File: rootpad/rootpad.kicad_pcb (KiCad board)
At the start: 2 copper layers, 76.2 x 99.2 mm, 56 parts, among them J1 USB_B_Mini, SW1 SW_Push, U1 ATmega32U4-AU, Y1 16MHz

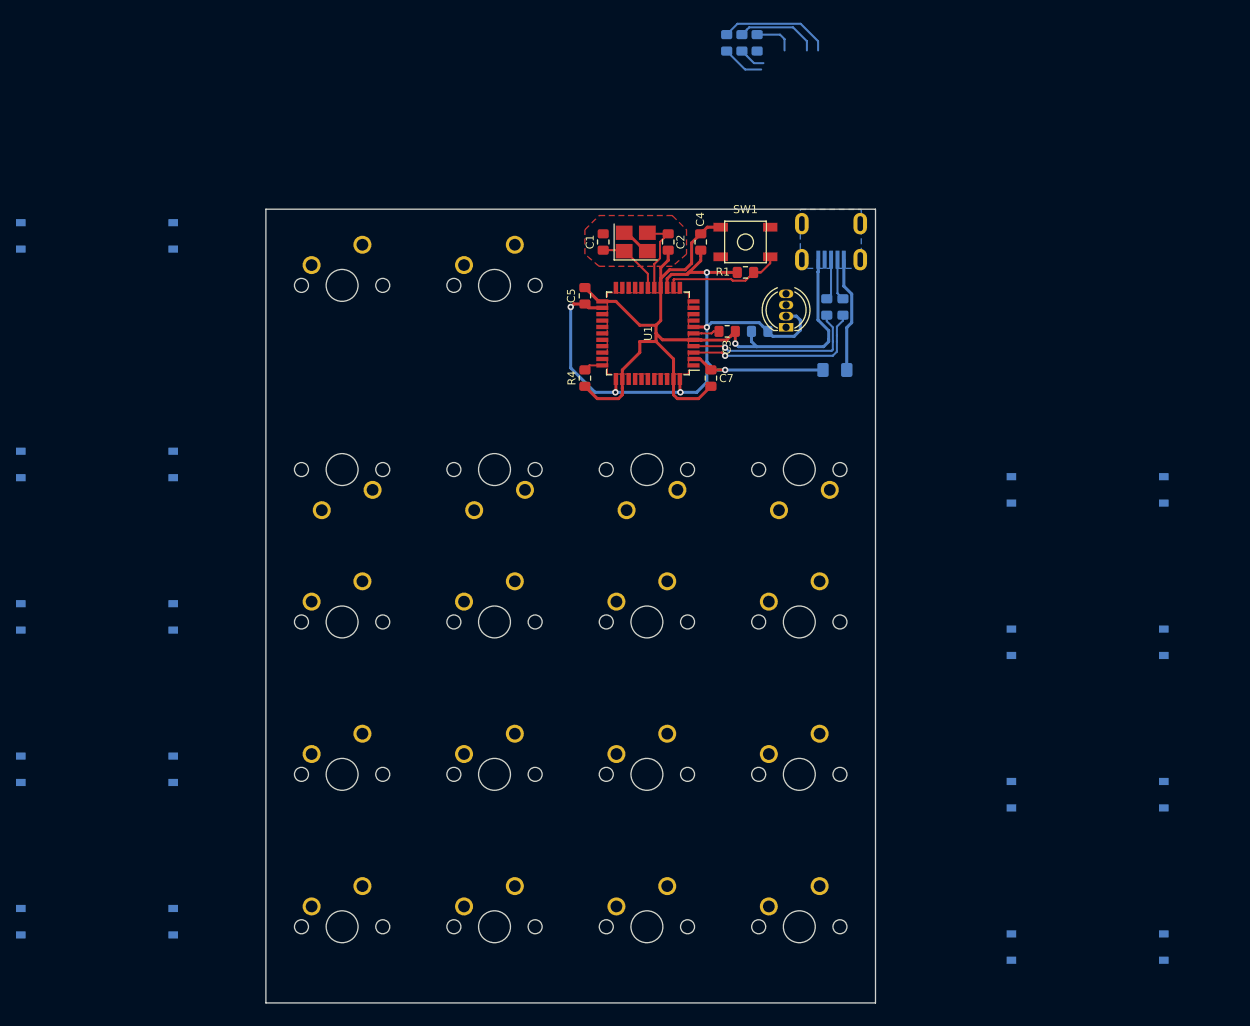
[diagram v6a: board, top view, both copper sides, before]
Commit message: Routed matrix and LED
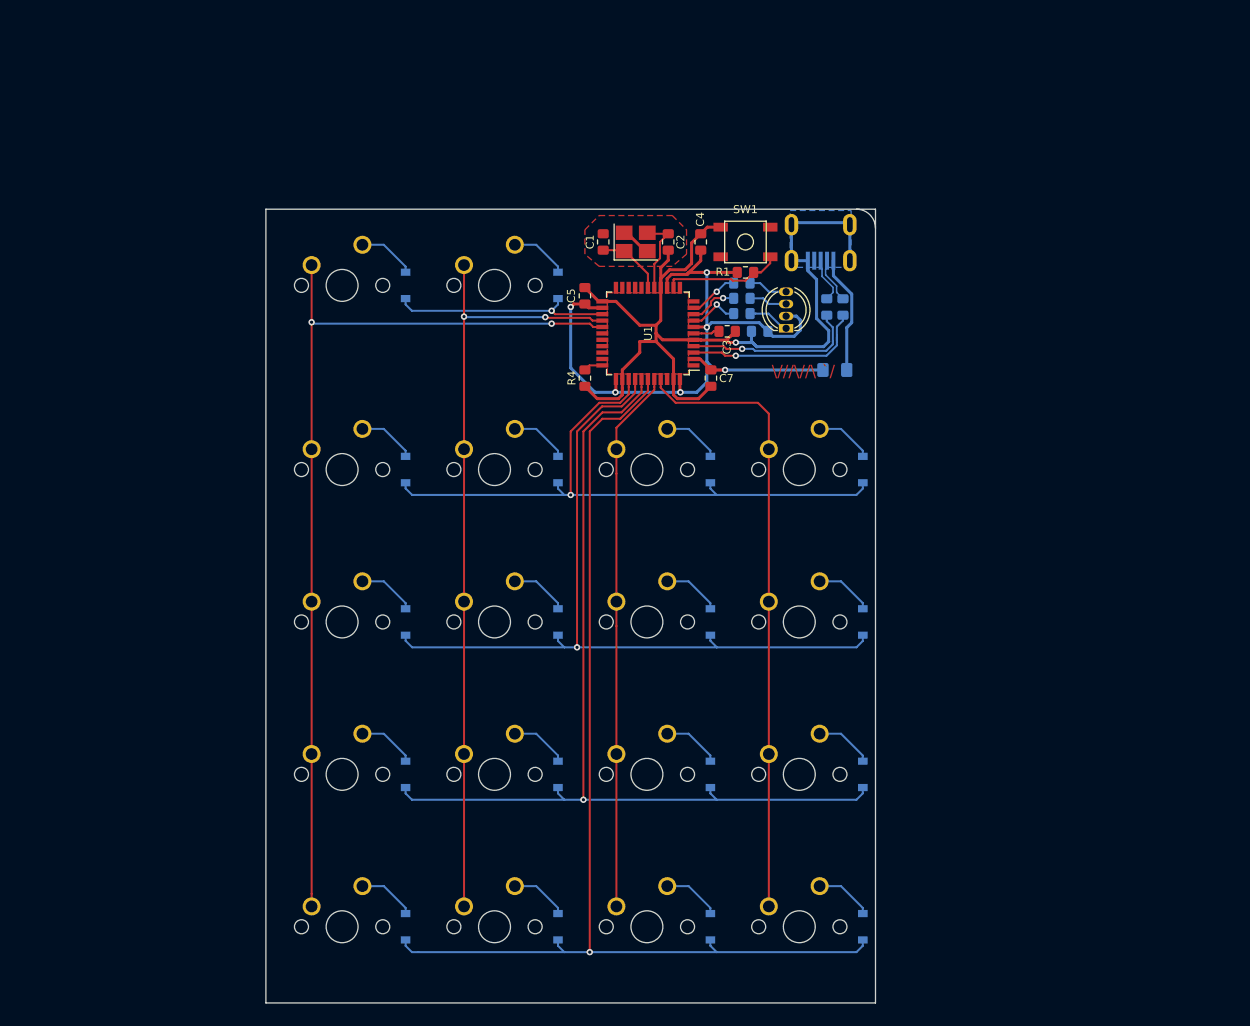
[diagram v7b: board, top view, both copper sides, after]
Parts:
- moved D1 48.5 mm to (138.1, 65.9)
- moved D2 48.5 mm to (157.2, 65.9)
- moved D11 48.1 mm to (138.1, 127.0)
- moved D15 48.1 mm to (138.1, 146.1)
- moved D3 48.1 mm to (138.1, 88.9)
- moved D7 48.1 mm to (138.1, 108.0)
- moved D12 48.1 mm to (157.2, 127.0)
- moved D16 48.1 mm to (157.2, 146.1)
- moved D4 48.1 mm to (157.2, 88.9)
- moved D8 48.1 mm to (157.2, 108.0)
- moved D10 37.7 mm to (195.3, 108.0)
- moved D13 37.7 mm to (176.2, 127.0)
- moved D14 37.7 mm to (195.3, 127.0)
- moved D18 37.7 mm to (195.3, 146.1)
- moved D6 37.7 mm to (195.3, 88.9)
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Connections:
- U1 pad 10: Net-(U1-Pad10) -> LED_B
- U1 pad 25: Net-(U1-Pad25) -> ROW0
- U1 pad 26: Net-(U1-Pad26) -> COL1
- U1 pad 27: Net-(U1-Pad27) -> COL0
- U1 pad 36: Net-(U1-Pad36) -> ROW1
- U1 pad 37: Net-(U1-Pad37) -> ROW2
- U1 pad 38: Net-(U1-Pad38) -> ROW3
- U1 pad 39: Net-(U1-Pad39) -> ROW4
- U1 pad 40: Net-(U1-Pad40) -> COL2
- U1 pad 41: Net-(U1-Pad41) -> COL3
- U1 pad 8: Net-(U1-Pad8) -> LED_R
- U1 pad 9: Net-(U1-Pad9) -> LED_G
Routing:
- net ROW4: track 0.00 -> 138.9 mm, vias 0 -> 1
- net ROW3: track 0.00 -> 120.0 mm, vias 0 -> 1
- net COL0: track 0.00 -> 116.8 mm, vias 0 -> 2
- net ROW2: track 0.00 -> 100.9 mm, vias 0 -> 1
- net COL1: track 0.00 -> 97.7 mm, vias 0 -> 2
- net ROW1: track 0.00 -> 82.0 mm, vias 0 -> 1
- net COL3: track 0.00 -> 77.6 mm
- net COL2: track 0.00 -> 67.9 mm
- net ROW0: track 0.00 -> 27.7 mm, vias 0 -> 1
- net GND: track 105.1 -> 123.5 mm
- net Net-(D19-Pad4): track 14.0 -> 4.95 mm
- net Net-(D2-Pad2): track 0.00 -> 7.23 mm
- net Net-(D1-Pad2): track 0.00 -> 7.23 mm
- net Net-(D18-Pad2): track 0.00 -> 7.23 mm
- net Net-(D17-Pad2): track 0.00 -> 7.23 mm
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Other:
- outline, holes or cut-outs redrawn
- board text added: "\///\//\ `/"

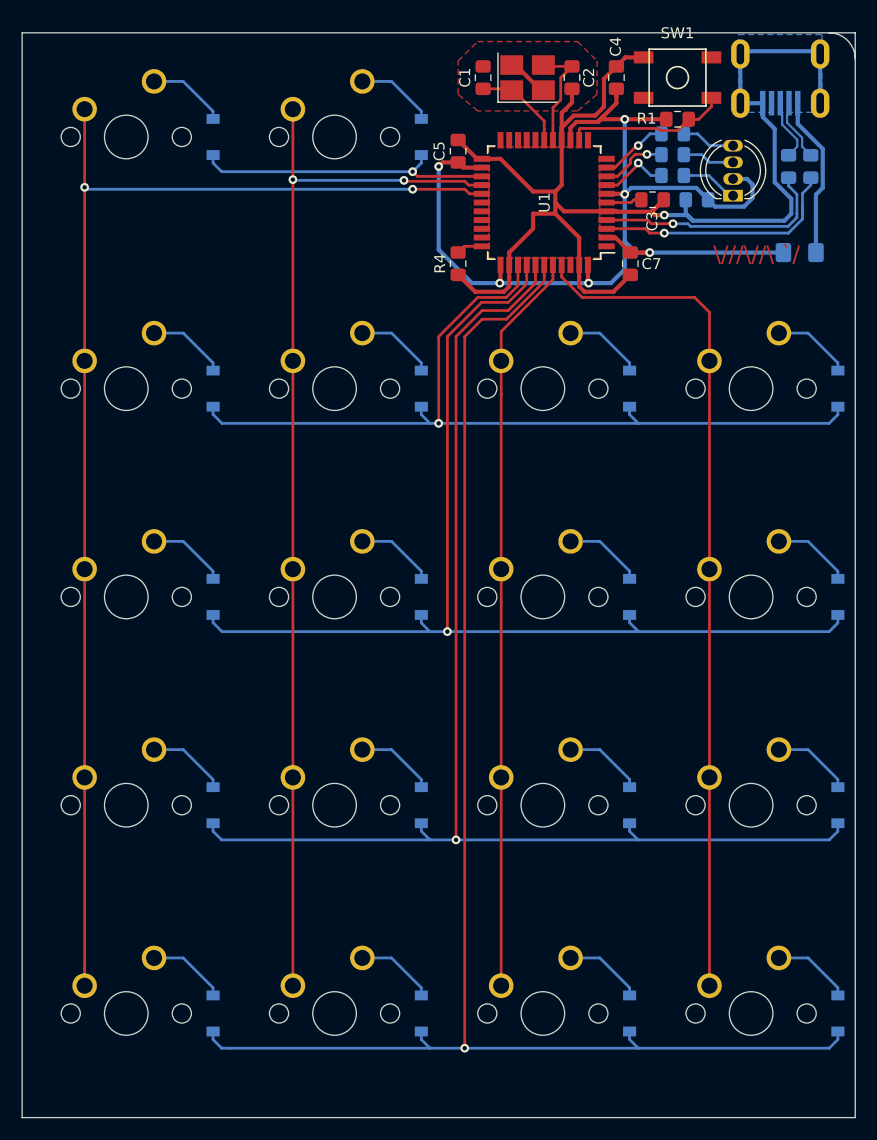
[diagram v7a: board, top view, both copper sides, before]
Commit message: Arranged silkscreen, placed holes
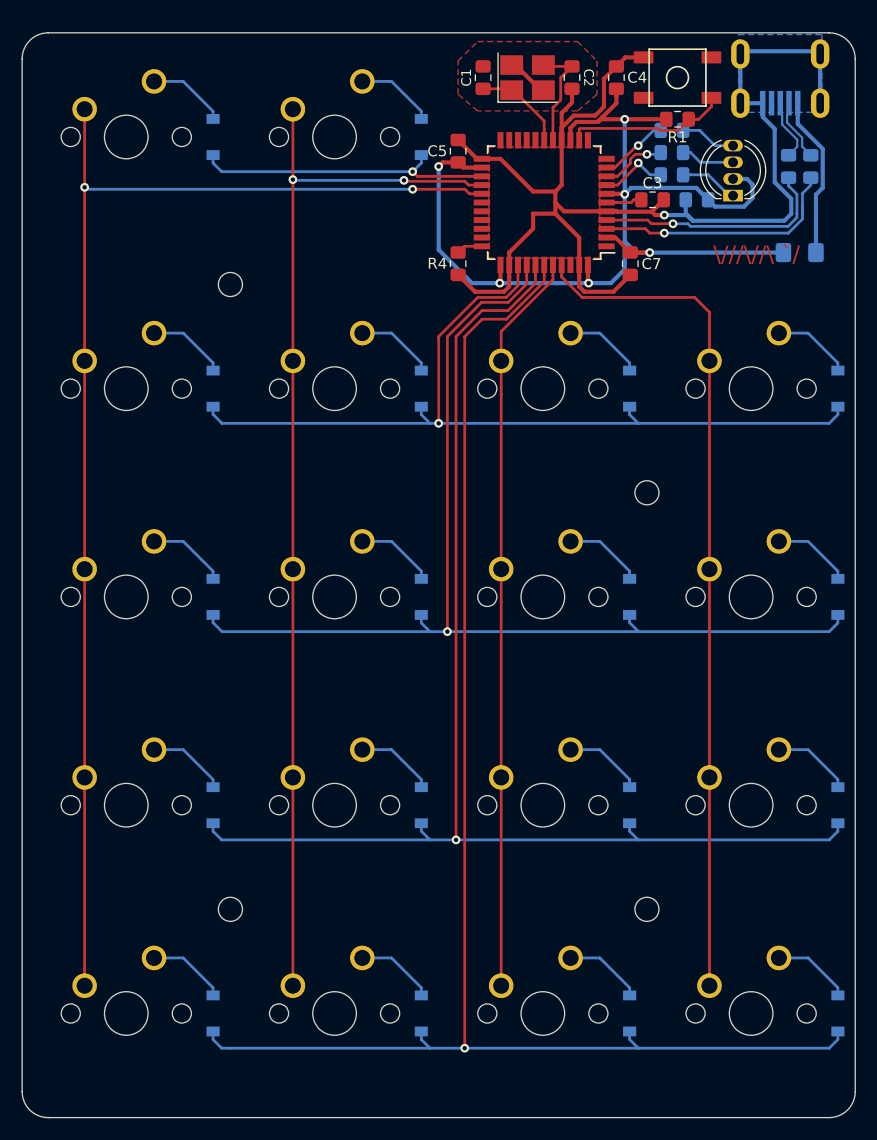
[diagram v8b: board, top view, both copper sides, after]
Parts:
- added REF**: MountingHole_2.2mm_M2, MountingHole:MountingHole_2.2mm_M2, F.Cu at (139.7, 79.4)
- added REF**: MountingHole_2.2mm_M2, MountingHole:MountingHole_2.2mm_M2, F.Cu at (177.8, 98.4)
- added REF**: MountingHole_2.2mm_M2, MountingHole:MountingHole_2.2mm_M2, F.Cu at (177.8, 136.5)
- added REF**: MountingHole_2.2mm_M2, MountingHole:MountingHole_2.2mm_M2, F.Cu at (139.7, 136.5)
- moved R7 0.32 mm to (180.1, 65.3)
- moved R6 0.20 mm to (180.1, 67.3)
- moved R5 0.09 mm to (180.1, 69.3)
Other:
- outline, holes or cut-outs redrawn
